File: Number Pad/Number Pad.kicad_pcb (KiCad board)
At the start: 2 copper layers, 44 parts, among them J1 Conn_01x05_Female, J2 Conn_01x05_Male

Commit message: Fixed issue with connector
accidentally had two Vcc on each connector
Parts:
- J1: footprint Connector_JST:JST_PH_S6B-PH-K_1x06_P2.00mm_Horizontal -> Connector_JST:JST_PH_S5B-PH-K_1x05_P2.00mm_Horizontal
- moved R1 5.67 mm to (39.7, 61.9), turned to -90 degrees
- moved J1 0.82 mm to (35.8, 58.7)
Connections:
- J1 pad 1: VCC -> +5V
- J2 pad 1: VCC -> +5V

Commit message: Started wiring
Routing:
- net COL3: track 0.00 -> 76.2 mm
- net COL2: track 0.00 -> 76.2 mm
- net COL0: track 0.00 -> 76.2 mm
- net COL1: track 0.00 -> 76.2 mm
- net ROW4: track 0.00 -> 66.2 mm
- net ROW3: track 0.00 -> 66.2 mm, vias 0 -> 6
- net ROW1: track 0.00 -> 66.2 mm, vias 0 -> 6
- net ROW0: track 0.00 -> 66.2 mm, vias 0 -> 6
- net ROW2: track 0.00 -> 66.2 mm, vias 0 -> 7
- net Net-(D9-Pad2): track 0.00 -> 7.51 mm
- net Net-(D4-Pad2): track 0.00 -> 7.51 mm
- net Net-(D19-Pad2): track 0.00 -> 7.51 mm
- net Net-(D14-Pad2): track 0.00 -> 7.51 mm
- net Net-(D6-Pad2): track 0.00 -> 7.51 mm
- net Net-(D16-Pad2): track 0.00 -> 7.51 mm
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
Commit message: Finished routing
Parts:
- removed R1, R2: 100, Resistor_SMD:R_0805_2012Metric
- J1: value Conn_01x05_Female -> Conn_01x19_Female; footprint Connector_JST:JST_PH_S5B-PH-K_1x05_P2.00mm_Horizontal -> Connector_JST:JST_SH_SM20B-SRSS-TB_1x20-1MP_P1.00mm_Horizontal
- J2: value Conn_01x05_Male -> Conn_01x19_Male; footprint Connector_JST:JST_PH_S5B-PH-K_1x05_P2.00mm_Horizontal -> Connector_JST:JST_SH_SM20B-SRSS-TB_1x20-1MP_P1.00mm_Horizontal
- moved J1 4.17 mm to (34.5, 62.7), turned to 90 degrees
- moved J2 3.97 mm to (120.7, 62.7), turned to -90 degrees
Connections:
- D1 pad 1: ROW0 -> ROW5
- D10 pad 1: ROW4 -> ROW9
- D11 pad 1: ROW0 -> ROW5
- D12 pad 1: ROW1 -> ROW6
- D13 pad 1: ROW2 -> ROW7
- D14 pad 1: ROW3 -> ROW8
- D15 pad 1: ROW4 -> ROW9
- D16 pad 1: ROW0 -> ROW5
- D17 pad 1: ROW1 -> ROW6
- D18 pad 1: ROW2 -> ROW7
- D19 pad 1: ROW3 -> ROW8
- D2 pad 1: ROW1 -> ROW6
- D20 pad 1: ROW4 -> ROW9
- D3 pad 1: ROW2 -> ROW7
- D4 pad 1: ROW3 -> ROW8
- D5 pad 1: ROW4 -> ROW9
- D6 pad 1: ROW0 -> ROW5
- D7 pad 1: ROW1 -> ROW6
- D8 pad 1: ROW2 -> ROW7
- D9 pad 1: ROW3 -> ROW8
- J1 pad 3: Net-(R1-Pad2) -> COL0
- J1 pad 4: unconnected-(J1-Pad4) -> COL1
- J1 pad 5: GND -> COL2
- J2 pad 3: Net-(J2-Pad3) -> COL0
- J2 pad 4: unconnected-(J2-Pad4) -> COL1
- J2 pad 5: GND -> COL2
- MX_*1 pad 1: COL2 -> COL6
- MX_+1 pad 1: COL3 -> COL7
- MX_-1 pad 1: COL3 -> COL7
- MX_.1 pad 1: COL2 -> COL6
- MX_/1 pad 1: COL1 -> COL5
- MX_0k1 pad 1: COL0 -> COL4
- MX_0k2 pad 1: COL1 -> COL5
- MX_1 pad 1: COL0 -> COL4
- MX_2 pad 1: COL1 -> COL5
- MX_3 pad 1: COL2 -> COL6
- MX_4 pad 1: COL0 -> COL4
- MX_5 pad 1: COL1 -> COL5
- MX_6 pad 1: COL2 -> COL6
- MX_7 pad 1: COL0 -> COL4
- MX_8 pad 1: COL1 -> COL5
- MX_9 pad 1: COL2 -> COL6
- MX_Bksp1 pad 1: COL3 -> COL7
- MX_Enter1 pad 1: COL3 -> COL7
- MX_Enter2 pad 1: COL3 -> COL7
- MX_Num_Lock1 pad 1: COL0 -> COL4
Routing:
- net ROW9: track 0.00 -> 185.7 mm, vias 0 -> 2
- net COL4: track 0.00 -> 184.3 mm, vias 0 -> 8
- net COL5: track 0.00 -> 181.1 mm, vias 0 -> 8
- net COL7: track 0.00 -> 180.6 mm, vias 0 -> 8
- net COL6: track 0.00 -> 180.5 mm, vias 0 -> 8
- net ROW5: track 0.00 -> 169.5 mm, vias 0 -> 10
- net ROW8: track 0.00 -> 144.9 mm, vias 0 -> 10
- net ROW6: track 0.00 -> 141.7 mm, vias 0 -> 10
- net GND: track 0.00 -> 126.2 mm, vias 0 -> 8
- net +5V: track 0.00 -> 107.8 mm, vias 0 -> 10
- net VCC: track 0.00 -> 106.6 mm, vias 0 -> 10
- net ROW7: track 0.00 -> 105.9 mm, vias 0 -> 11
- net COL10: track 0.00 -> 97.1 mm, vias 0 -> 8
- net COL9: track 0.00 -> 94.9 mm, vias 0 -> 16
- net COL8: track 0.00 -> 93.1 mm, vias 0 -> 16
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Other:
- board outline added: 92.9 x 95.2 mm

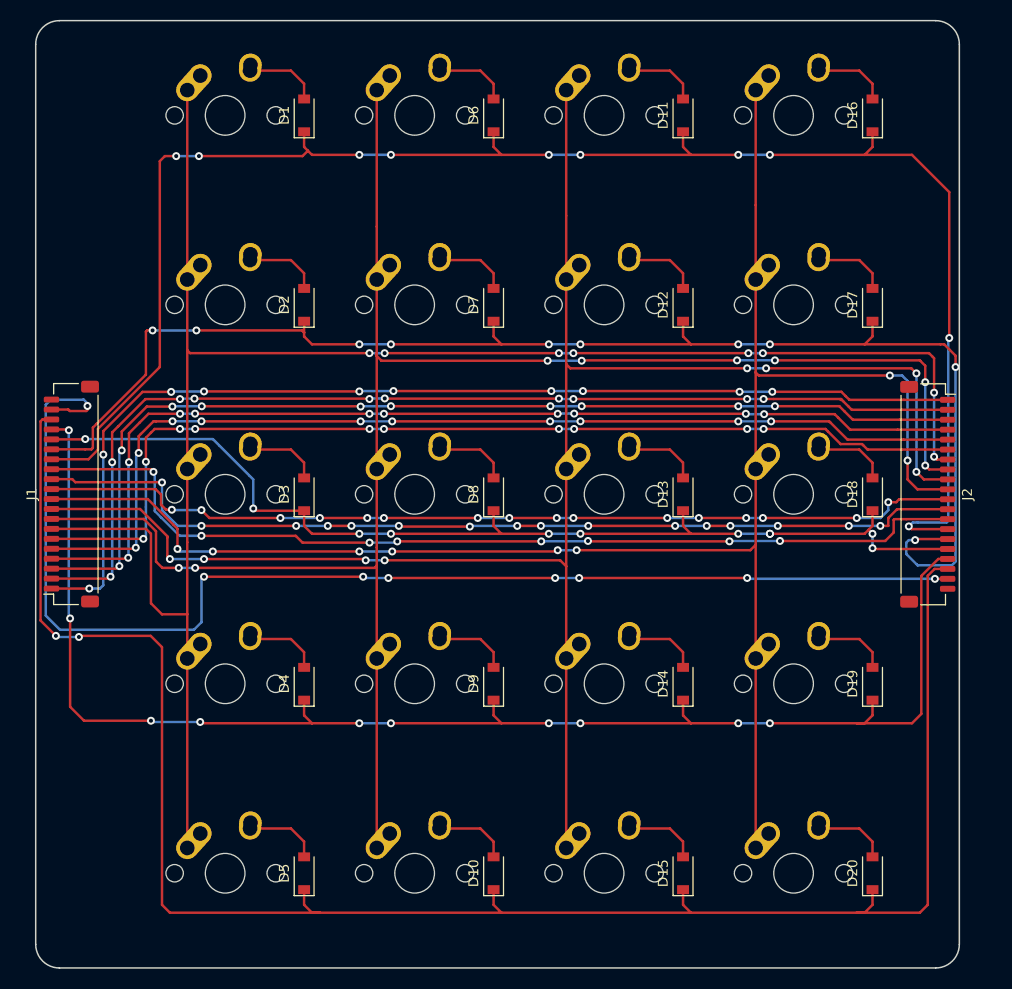
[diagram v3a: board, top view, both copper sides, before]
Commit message: Added ground fill
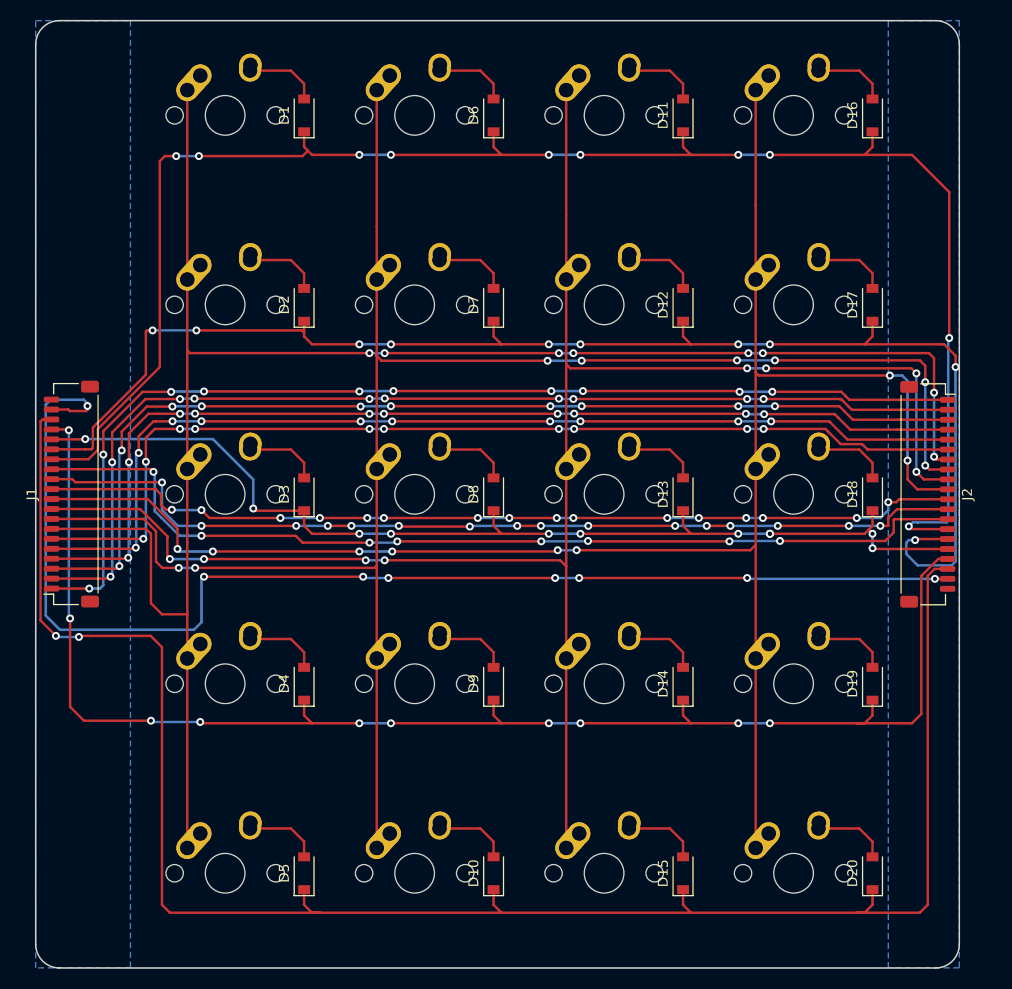
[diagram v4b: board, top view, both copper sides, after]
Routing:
- added copper zone on B.Cu, net GND
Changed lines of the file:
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@@
   (segment (start 42.926 64.389) (end 42.926 60.706) (width 0.25) (layer "B.Cu") (net 39))
   (segment (start 45.485112 66.880753) (end 45.417753 66.880753) (width 0.25) (layer "B.Cu") (net 39))
+  (zone (net 28) (net_name "GND") (layer "B.Cu") (hatch edge 0.508)
+    (connect_pads (clearance 0.508))
+    (min_thickness 0.254) (filled_areas_thickness no)
+    (fill yes (thermal_gap 0.508) (thermal_bridge_width 0.508))
+    (polygon
+      (pts
+        (xy 123.825 110.33125)
+        (xy 116.68125 110.33125)
+        (xy 116.68125 15.08125)
+        (xy 123.825 15.08125)
+      )
+    )
+  )
+  (zone (net 28) (net_name "GND") (layer "B.Cu") (hatch edge 0.508)
+    (connect_pads (clearance 0.508))
+    (min_thickness 0.254) (filled_areas_thickness no)
+    (fill yes (thermal_gap 0.508) (thermal_bridge_width 0.508))
+    (polygon
+      (pts
+        (xy 40.48125 110.33125)
+        (xy 30.95625 110.33125)
+        (xy 30.95625 15.08125)
+        (xy 40.48125 15.08125)
+      )
+    )
+  )
 )
